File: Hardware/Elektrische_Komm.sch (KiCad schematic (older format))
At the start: 136 parts, among them J1 Conn_01x01, J2 Conn_01x01, J3 Conn_01x01, J4 Conn_01x04, J5 USB_OTG, Q1 BSZ014NE2LS5IF, Q10 BSR202NL6327HTSA1, Q11 BSR202NL6327HTSA1, Q12 BSR202NL6327HTSA1, Q13 BSR202NL6327HTSA1, Q14 BSR202NL6327HTSA1, Q2 BSZ014NE2LS5IF, Q3 BSZ014NE2LS5IF, Q4 BSZ014NE2LS5IF, Q5 BSZ014NE2LS5IF, Q6 BSZ014NE2LS5IF, Q7 BSR202NL6327HTSA1, Q8 BSR202NL6327HTSA1, Q9 BSR202NL6327HTSA1, SW1 SW_Push, SW2 SW_Push, U1 TS374IDT, U10 TPS561201, U11 LVM339IDT, U12 STM32F413R(G-H)Tx_u, U2 UCC27710, U3 ACS723LLCTR, U4 UCC27710, U5 ACS723LLCTR, U6 UCC27710, U7 74HC32D, U8 74LVC2G02, U9 LDK715M50R, Y1 10MHz

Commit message: Layout
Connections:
- net +3V3: now also U7.14; no longer U7.14
- net GNDREF: now also U7.7; no longer U7.7
- net OR1: now also U7.11; no longer U7.6
- net OR2: now also U7.6; no longer U7.11
- net at R22.2, U11.2: now also U7.12; no longer U7.4
- net at R28.2, U11.1: now also U7.13; no longer U7.5
- net at R32.2, U11.14: now also U7.4; no longer U7.12
- net at R40.2, U11.13: now also U7.5; no longer U7.13
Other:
- moved on the sheet: U7B, U7D
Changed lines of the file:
@@
 L 74HC32D U7
 U 2 1 5AF6CFE2
-P 3850 7150
-F 0 "U7" H 4100 7050 60  0000 C CNN
-F 1 "74HC32D" H 4200 6950 60  0000 C CNN
-F 2 "Housings_SSOP:TSSOP-14_4.4x5mm_Pitch0.65mm" H 3850 7150 60  0001 C CNN
-F 3 "" H 3850 7150 60  0001 C CNN
-	2    3850 7150
+P 4000 11350
+F 0 "U7" H 4250 11250 60  0000 C CNN
+F 1 "74HC32D" H 4350 11150 60  0000 C CNN
+F 2 "Housings_SSOP:TSSOP-14_4.4x5mm_Pitch0.65mm" H 4000 11350 60  0001 C CNN
+F 3 "" H 4000 11350 60  0001 C CNN
+	2    4000 11350
 	1    0    0    -1
 $EndComp
@@
 L 74HC32D U7
 U 4 1 5AF711A3
-P 4000 11350
-F 0 "U7" H 4050 11250 60  0000 C CNN
-F 1 "74HC32D" H 4000 11150 60  0000 C CNN
-F 2 "Housings_SSOP:TSSOP-14_4.4x5mm_Pitch0.65mm" H 4000 11350 60  0001 C CNN
-F 3 "" H 4000 11350 60  0001 C CNN
-	4    4000 11350
+P 3850 7150
+F 0 "U7" H 3900 7050 60  0000 C CNN
+F 1 "74HC32D" H 3850 6950 60  0000 C CNN
+F 2 "Housings_SSOP:TSSOP-14_4.4x5mm_Pitch0.65mm" H 3850 7150 60  0001 C CNN
+F 3 "" H 3850 7150 60  0001 C CNN
+	4    3850 7150
 	1    0    0    -1
 $EndComp
@@
 	0    1    1    0
 $EndComp
+$Comp
+L USBLC6-2SC6Y D4
+U 1 1 5B005011
+P 14400 3700
+F 0 "D4" H 14400 3700 60  0000 C CNN
+F 1 "USBLC6-2SC6Y" H 14350 3600 60  0000 C CNN
+F 2 "TO_SOT_Packages_SMD:SOT-23-6" H 14400 3700 60  0001 C CNN
+F 3 "" H 14400 3700 60  0001 C CNN
+	1    14400 3700
+	1    0    0    -1
+$EndComp
+$Comp
+L GNDREF #PWR099
+U 1 1 5B005DAE
+P 13800 3500
+F 0 "#PWR099" H 13800 3250 50  0001 C CNN
+F 1 "GNDREF" H 13800 3350 50  0001 C CNN
+F 2 "" H 13800 3500 50  0001 C CNN
+F 3 "" H 13800 3500 50  0001 C CNN
+	1    13800 3500
+	0    1    1    0
+$EndComp
+$Comp
+L TEST TP18
+U 1 1 5B06AA0D
+P 2400 15200
+F 0 "TP18" H 2400 15500 50  0000 C BNN
+F 1 "TEST" H 2400 15450 50  0000 C CNN
+F 2 "Pin_Headers:Pin_Header_Straight_1x01_Pitch1.00mm" H 2400 15200 50  0001 C CNN
+F 3 "" H 2400 15200 50  0001 C CNN
+	1    2400 15200
+	0    -1   -1   0
+$EndComp
+Text Label 2650 15200 0    61   ~ 0
+SYSCLK_OUT
+$Comp
+L +3.3V #PWR0100
+U 1 1 5B073ADE
+P 11950 8050
+F 0 "#PWR0100" H 11950 7900 50  0001 C CNN
+F 1 "+3.3V" H 11950 8190 50  0000 C CNN
+F 2 "" H 11950 8050 50  0001 C CNN
+F 3 "" H 11950 8050 50  0001 C CNN
+	1    11950 8050
+	1    0    0    -1
+$EndComp
+$Comp
+L +3.3V #PWR0101
+U 1 1 5B073CAB
+P 12050 8250
+F 0 "#PWR0101" H 12050 8100 50  0001 C CNN
+F 1 "+3.3V" H 12050 8390 50  0000 C CNN
+F 2 "" H 12050 8250 50  0001 C CNN
+F 3 "" H 12050 8250 50  0001 C CNN
+	1    12050 8250
+	1    0    0    -1
+$EndComp
+$Comp
+L +3.3V #PWR0102
+U 1 1 5B074042
+P 12050 8500
+F 0 "#PWR0102" H 12050 8350 50  0001 C CNN
+F 1 "+3.3V" H 12050 8640 50  0000 C CNN
+F 2 "" H 12050 8500 50  0001 C CNN
+F 3 "" H 12050 8500 50  0001 C CNN
+	1    12050 8500
+	1    0    0    -1
+$EndComp
+$Comp
+L +3.3V #PWR0103
+U 1 1 5B07420F
+P 12050 8750
+F 0 "#PWR0103" H 12050 8600 50  0001 C CNN
+F 1 "+3.3V" H 12050 8890 50  0000 C CNN
+F 2 "" H 12050 8750 50  0001 C CNN
+F 3 "" H 12050 8750 50  0001 C CNN
+	1    12050 8750
+	-1   0    0    1
+$EndComp
+$Comp
+L +3.3V #PWR0104
+U 1 1 5B0745A8
+P 11900 8950
+F 0 "#PWR0104" H 11900 8800 50  0001 C CNN
+F 1 "+3.3V" H 11900 9090 50  0000 C CNN
+F 2 "" H 11900 8950 50  0001 C CNN
+F 3 "" H 11900 8950 50  0001 C CNN
+	1    11900 8950
+	0    -1   -1   0
+$EndComp
+$Comp
+L C C50
+U 1 1 5B073098
+P 2000 2800
+F 0 "C50" H 2025 2900 50  0000 L CNN
+F 1 "100n" H 2025 2700 50  0000 L CNN
+F 2 "Capacitors_SMD:C_0603" H 2038 2650 50  0001 C CNN
+F 3 "" H 2000 2800 50  0001 C CNN
+	1    2000 2800
+	0    1    1    0
+$EndComp
+$Comp
+L GNDREF #PWR0105
+U 1 1 5B0735C2
+P 1650 2800
+F 0 "#PWR0105" H 1650 2550 50  0001 C CNN
+F 1 "GNDREF" H 1650 2650 50  0000 C CNN
+F 2 "" H 1650 2800 50  0001 C CNN
+F 3 "" H 1650 2800 50  0001 C CNN
+	1    1650 2800
+	0    1    1    0
+$EndComp
+$Comp
+L GNDREF #PWR0106
+U 1 1 5B074522
+P 1800 3900
+F 0 "#PWR0106" H 1800 3650 50  0001 C CNN
+F 1 "GNDREF" H 1800 3750 50  0000 C CNN
+F 2 "" H 1800 3900 50  0001 C CNN
+F 3 "" H 1800 3900 50  0001 C CNN
+	1    1800 3900
+	1    0    0    -1
+$EndComp
+$Comp
+L C C51
+U 1 1 5B074528
+P 2200 4450
+F 0 "C51" H 2225 4550 50  0000 L CNN
+F 1 "100n" H 2225 4350 50  0000 L CNN
+F 2 "Capacitors_SMD:C_0603" H 2238 4300 50  0001 C CNN
+F 3 "" H 2200 4450 50  0001 C CNN
+	1    2200 4450
+	0    1    1    0
+$EndComp
+$Comp
+L GNDREF #PWR0107
+U 1 1 5B07452F
+P 1850 4450
+F 0 "#PWR0107" H 1850 4200 50  0001 C CNN
+F 1 "GNDREF" H 1850 4300 50  0000 C CNN
+F 2 "" H 1850 4450 50  0001 C CNN
+F 3 "" H 1850 4450 50  0001 C CNN
+	1    1850 4450
+	0    1    1    0
+$EndComp
 Wire Notes Line
 	5400 450  5400 5950
@@
 	3200 6650 3200 6600
 Wire Wire Line
-	3200 6600 3450 6600
-Wire Wire Line
 	3100 8450 3100 6900
-Wire Wire Line
-	3100 6900 3450 6900
 Wire Wire Line
 	3450 12050 3450 11100
@@
 Wire Wire Line
 	12600 3200 12550 3200
-$Comp
-L USBLC6-2SC6Y D4
-U 1 1 5B005011
-P 14400 3700
-F 0 "D4" H 14400 3700 60  0000 C CNN
-F 1 "USBLC6-2SC6Y" H 14350 3600 60  0000 C CNN
-F 2 "TO_SOT_Packages_SMD:SOT-23-6" H 14400 3700 60  0001 C CNN
-F 3 "" H 14400 3700 60  0001 C CNN
-	1    14400 3700
-	1    0    0    -1
-$EndComp
 Wire Wire Line
 	13800 3500 13900 3500
-$Comp
-L GNDREF #PWR099
-U 1 1 5B005DAE
-P 13800 3500
-F 0 "#PWR099" H 13800 3250 50  0001 C CNN
-F 1 "GNDREF" H 13800 3350 50  0001 C CNN
-F 2 "" H 13800 3500 50  0001 C CNN
-F 3 "" H 13800 3500 50  0001 C CNN
-	1    13800 3500
-	0    1    1    0
-$EndComp
 Wire Wire Line
 	14800 3400 15050 3400
 Wire Wire Line
 	14800 3600 15050 3600
-$Comp
-L TEST TP18
-U 1 1 5B06AA0D
-P 2400 15200
-F 0 "TP18" H 2400 15500 50  0000 C BNN
-F 1 "TEST" H 2400 15450 50  0000 C CNN
-F 2 "Pin_Headers:Pin_Header_Straight_1x01_Pitch1.00mm" H 2400 15200 50  0001 C CNN
-F 3 "" H 2400 15200 50  0001 C CNN
-	1    2400 15200
-	0    -1   -1   0
-$EndComp
-Text Label 2650 15200 0    61   ~ 0
-SYSCLK_OUT
 Wire Wire Line
 	2650 15200 2400 15200
-$Comp
-L +3.3V #PWR0100
-U 1 1 5B073ADE
-P 11950 8050
-F 0 "#PWR0100" H 11950 7900 50  0001 C CNN
-F 1 "+3.3V" H 11950 8190 50  0000 C CNN
-F 2 "" H 11950 8050 50  0001 C CNN
-F 3 "" H 11950 8050 50  0001 C CNN
-	1    11950 8050
-	1    0    0    -1
-$EndComp
-$Comp
-L +3.3V #PWR0101
-U 1 1 5B073CAB
-P 12050 8250
-F 0 "#PWR0101" H 12050 8100 50  0001 C CNN
-F 1 "+3.3V" H 12050 8390 50  0000 C CNN
-F 2 "" H 12050 8250 50  0001 C CNN
-F 3 "" H 12050 8250 50  0001 C CNN
-	1    12050 8250
-	1    0    0    -1
-$EndComp
-$Comp
-L +3.3V #PWR0102
-U 1 1 5B074042
-P 12050 8500
-F 0 "#PWR0102" H 12050 8350 50  0001 C CNN
-F 1 "+3.3V" H 12050 8640 50  0000 C CNN
-F 2 "" H 12050 8500 50  0001 C CNN
-F 3 "" H 12050 8500 50  0001 C CNN
-	1    12050 8500
-	1    0    0    -1
-$EndComp
-$Comp
-L +3.3V #PWR0103
-U 1 1 5B07420F
-P 12050 8750
-F 0 "#PWR0103" H 12050 8600 50  0001 C CNN
-F 1 "+3.3V" H 12050 8890 50  0000 C CNN
-F 2 "" H 12050 8750 50  0001 C CNN
-F 3 "" H 12050 8750 50  0001 C CNN
-	1    12050 8750
-	-1   0    0    1
-$EndComp
-$Comp
-L +3.3V #PWR0104
-U 1 1 5B0745A8
-P 11900 8950
-F 0 "#PWR0104" H 11900 8800 50  0001 C CNN
-F 1 "+3.3V" H 11900 9090 50  0000 C CNN
-F 2 "" H 11900 8950 50  0001 C CNN
-F 3 "" H 11900 8950 50  0001 C CNN
-	1    11900 8950
-	0    -1   -1   0
-$EndComp
 Connection ~ 12000 8950
 Wire Wire Line
@@
 Wire Wire Line
 	13300 3600 13900 3600
-$Comp
-L C C50
-U 1 1 5B073098
-P 2000 2800
-F 0 "C50" H 2025 2900 50  0000 L CNN
-F 1 "100n" H 2025 2700 50  0000 L CNN
-F 2 "Capacitors_SMD:C_0603" H 2038 2650 50  0001 C CNN
-F 3 "" H 2000 2800 50  0001 C CNN
-	1    2000 2800
-	0    1    1    0
-$EndComp
 Wire Wire Line
 	2550 2800 2150 2800
-$Comp
-L GNDREF #PWR?
-U 1 1 5B0735C2
-P 1650 2800
-F 0 "#PWR?" H 1650 2550 50  0001 C CNN
-F 1 "GNDREF" H 1650 2650 50  0000 C CNN
-F 2 "" H 1650 2800 50  0001 C CNN
-F 3 "" H 1650 2800 50  0001 C CNN
-	1    1650 2800
-	0    1    1    0
-$EndComp
 Wire Wire Line
 	1650 2800 1850 2800
-$Comp
-L GNDREF #PWR?
-U 1 1 5B074522
-P 1800 3900
-F 0 "#PWR?" H 1800 3650 50  0001 C CNN
-F 1 "GNDREF" H 1800 3750 50  0000 C CNN
-F 2 "" H 1800 3900 50  0001 C CNN
-F 3 "" H 1800 3900 50  0001 C CNN
-	1    1800 3900
-	1    0    0    -1
-$EndComp
-$Comp
-L C C51
-U 1 1 5B074528
-P 2200 4450
-F 0 "C51" H 2225 4550 50  0000 L CNN
-F 1 "100n" H 2225 4350 50  0000 L CNN
-F 2 "Capacitors_SMD:C_0603" H 2238 4300 50  0001 C CNN
-F 3 "" H 2200 4450 50  0001 C CNN
-	1    2200 4450
-	0    1    1    0
-$EndComp
 Wire Wire Line
 	2750 4450 2350 4450
-$Comp
-L GNDREF #PWR?
-U 1 1 5B07452F
-P 1850 4450
-F 0 "#PWR?" H 1850 4200 50  0001 C CNN
-F 1 "GNDREF" H 1850 4300 50  0000 C CNN
-F 2 "" H 1850 4450 50  0001 C CNN
-F 3 "" H 1850 4450 50  0001 C CNN
-	1    1850 4450
-	0    1    1    0
-$EndComp
 Wire Wire Line
 	1850 4450 2050 4450
+Wire Wire Line
+	3100 6900 3450 6900
+Wire Wire Line
+	3200 6600 3450 6600
 $EndSCHEMATC

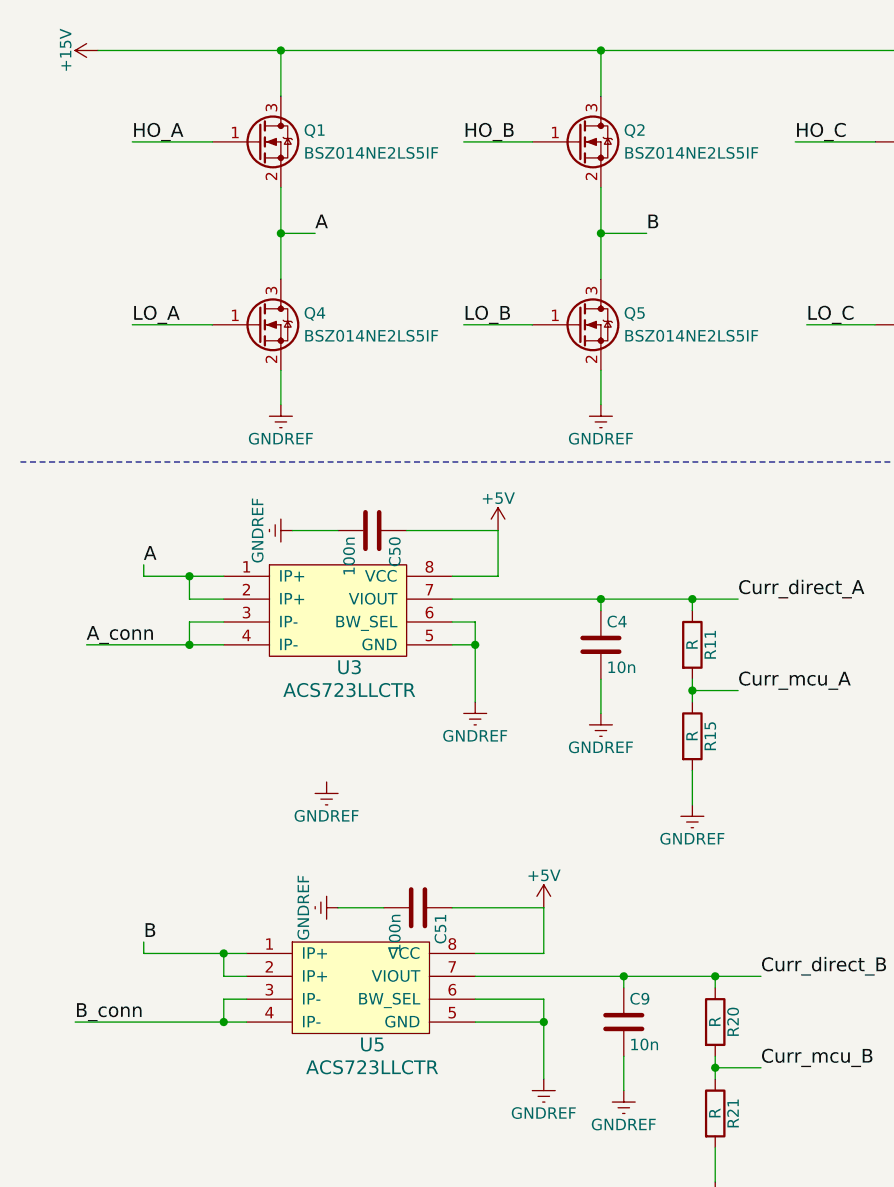
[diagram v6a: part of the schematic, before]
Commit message: Korrektur Strommessung
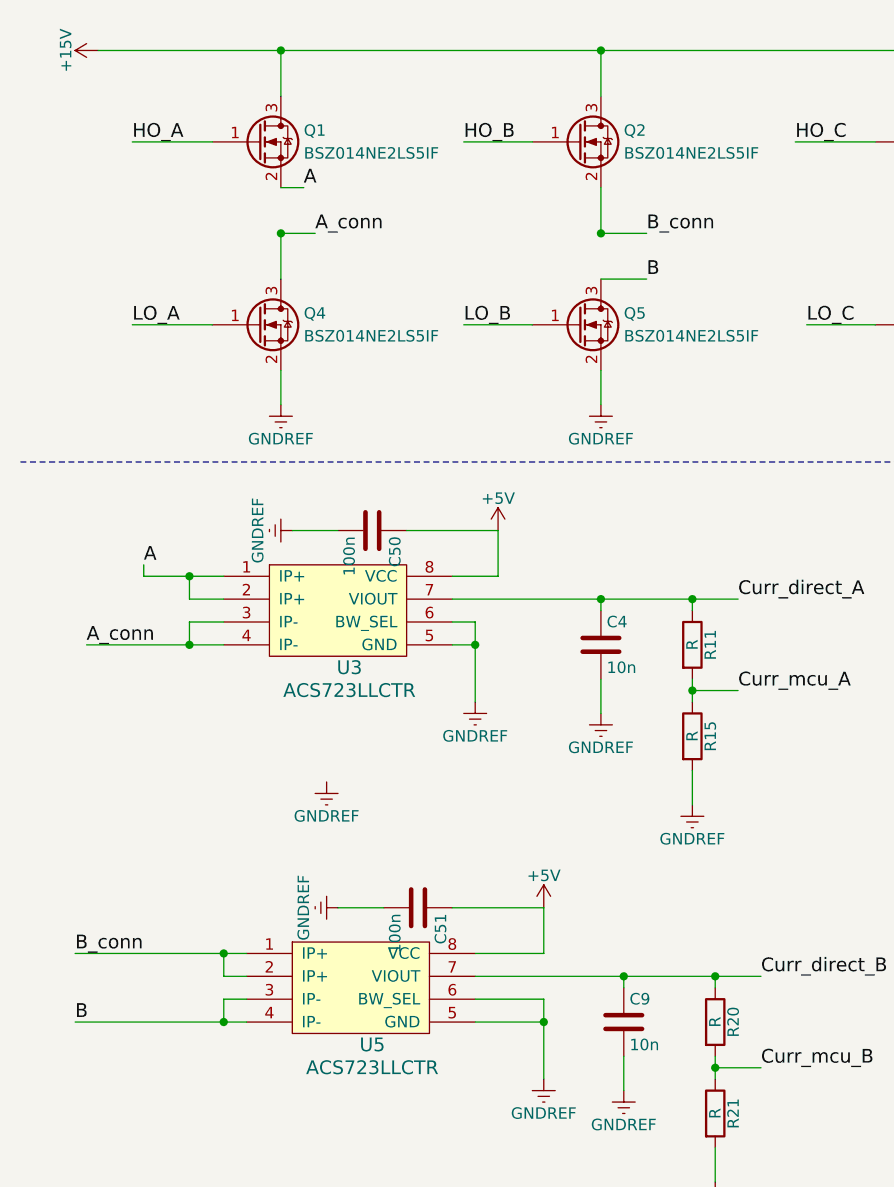
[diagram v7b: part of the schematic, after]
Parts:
- J1, J2, J3: footprint (none) -> kicadBibs:MotorConn
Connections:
- net A: no longer Q4.3 (D)
- net A_conn: now also Q4.3 (D)
- net B: now also U5.3 (IP-), U5.4 (IP-); no longer Q2.2 (S), U5.1 (IP+), U5.2 (IP+)
- net B_conn: now also Q2.2 (S), U5.1 (IP+), U5.2 (IP+); no longer U5.3 (IP-), U5.4 (IP-)
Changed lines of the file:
@@
 $EndComp
 Text Label 1750 1500 0    60   ~ 0
-A
-Text Label 3200 1500 0    60   ~ 0
+A_conn
+Text Label 3200 1700 0    60   ~ 0
 B
 Text Label 4700 1500 0    60   ~ 0
@@
 Text Label 1000 2950 0    60   ~ 0
 A
-Text Label 1000 4600 0    60   ~ 0
+Text Label 700  4950 0    60   ~ 0
 B
 Text Label 750  3300 0    60   ~ 0
 A_conn
-Text Label 700  4950 0    60   ~ 0
+Text Label 700  4650 0    60   ~ 0
 B_conn
 $Comp
@@
 F 0 "J1" H 12300 1000 50  0000 C CNN
 F 1 "Conn_01x01" H 12300 800 50  0000 C CNN
-F 2 "" H 12300 900 50  0001 C CNN
+F 2 "kicadBibs:MotorConn" H 12300 900 50  0001 C CNN
 F 3 "" H 12300 900 50  0001 C CNN
 	1    12300 900
@@
 F 0 "J2" H 12300 1300 50  0000 C CNN
 F 1 "Conn_01x01" H 12300 1100 50  0000 C CNN
-F 2 "" H 12300 1200 50  0001 C CNN
+F 2 "kicadBibs:MotorConn" H 12300 1200 50  0001 C CNN
 F 3 "" H 12300 1200 50  0001 C CNN
 	1    12300 1200
@@
 F 0 "J3" H 12300 1600 50  0000 C CNN
 F 1 "Conn_01x01" H 12300 1400 50  0000 C CNN
-F 2 "" H 12300 1500 50  0001 C CNN
+F 2 "kicadBibs:MotorConn" H 12300 1500 50  0001 C CNN
 F 3 "" H 12300 1500 50  0001 C CNN
 	1    12300 1500
@@
 	5400 450  5400 5950
 Wire Wire Line
-	1600 1300 1600 1700
-Wire Wire Line
-	3000 1300 3000 1700
-Wire Wire Line
 	4500 1300 4500 1700
 Wire Notes Line
@@
 Connection ~ 4500 1500
 Wire Wire Line
-	1000 4600 1000 4650
-Wire Wire Line
-	1000 4650 1450 4650
-Wire Wire Line
 	1450 4750 1350 4750
 Wire Wire Line
@@
 Wire Wire Line
 	3200 6600 3450 6600
+Wire Wire Line
+	1600 1500 1600 1700
+Text Label 1700 1300 0    60   ~ 0
+A
+Wire Wire Line
+	1700 1300 1600 1300
+Wire Wire Line
+	3000 1500 3000 1300
+Text Label 3200 1500 0    60   ~ 0
+B_conn
+Wire Wire Line
+	3200 1700 3000 1700
+Wire Wire Line
+	700  4650 1450 4650
 $EndSCHEMATC

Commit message: Zwei Strommesser
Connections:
- net Hochlauf: now also U12.56 (PB4/CAN3_TX/I2C3_SDA/I2S3_ext_SD/SAI1_SCK_A/SDIO_D0/SPI1_MISO/SPI3_MISO/SYS_JTRST/TIM3_CH1/UART7_TX); no longer U12.55 (PB3/CAN3_RX/FMPI2C1_SDA/I2C2_SDA/I2S1_CK/I2S3_CK/SAI1_SD_A/SPI1_SCK/SPI3_SCK/SYS_JTDO-SWO/TIM2_CH2/UART7_RX/USART1_RX)
- net LI_A: now also U12.16 (PA2/ADC1_IN2/FSMC_D4/FSMC_DA4/I2S_CKIN/TIM2_CH3/TIM5_CH3/TIM9_CH1/USART2_TX); no longer U12.14 (PA0/ADC1_IN0/SYS_WKUP1/TIM2_CH1/TIM2_ETR/TIM5_CH1/TIM8_ETR/UART4_TX/USART2_CTS)
- net LI_C: now also U12.14 (PA0/ADC1_IN0/SYS_WKUP1/TIM2_CH1/TIM2_ETR/TIM5_CH1/TIM8_ETR/UART4_TX/USART2_CTS); no longer U12.16 (PA2/ADC1_IN2/FSMC_D4/FSMC_DA4/I2S_CKIN/TIM2_CH3/TIM5_CH3/TIM9_CH1/USART2_TX)
- net elekKomm: now also U12.55 (PB3/CAN3_RX/FMPI2C1_SDA/I2C2_SDA/I2S1_CK/I2S3_CK/SAI1_SD_A/SPI1_SCK/SPI3_SCK/SYS_JTDO-SWO/TIM2_CH2/UART7_RX/USART1_RX); no longer U12.56 (PB4/CAN3_TX/I2C3_SDA/I2S3_ext_SD/SAI1_SCK_A/SDIO_D0/SPI1_MISO/SPI3_MISO/SYS_JTRST/TIM3_CH1/UART7_TX)
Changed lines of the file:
@@
 Text Label 16900 10100 0    61   ~ 0
 SYSCLK_OUT
-Text Label 17050 12950 0    61   ~ 0
+Text Label 17050 13150 0    61   ~ 0
 LI_A
 Text Label 17050 13050 0    61   ~ 0
 LI_B
-Text Label 17050 13150 0    61   ~ 0
+Text Label 17050 12950 0    61   ~ 0
 LI_C
 Text Label 17300 11150 0    61   ~ 0
@@
 Text Label 17050 13950 0    60   ~ 0
 Bemf_C
+Text Label 17450 11550 2    60   ~ 0
+Hochlauf
 Text Label 17450 11450 2    60   ~ 0
-Hochlauf
-Text Label 17450 11550 2    60   ~ 0
 elekKomm
 $Comp
